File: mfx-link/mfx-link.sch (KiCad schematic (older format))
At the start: 53 parts, among them P1 CONN_01X02, P2 CONN_02X03, P3 CONN_01X02, P4 Grove I2C, P5 IBT-2, P6 CONN_01X02, P7 CONN_01X03, P8 Grove UART, P9 MFX, Q1 BC547, Q2 BC547, Q3 BC547, SW1 SW_PUSH, U1 LM393-1, U2 7805, U3 PIC16F1705, U4 6N137, U5 7805

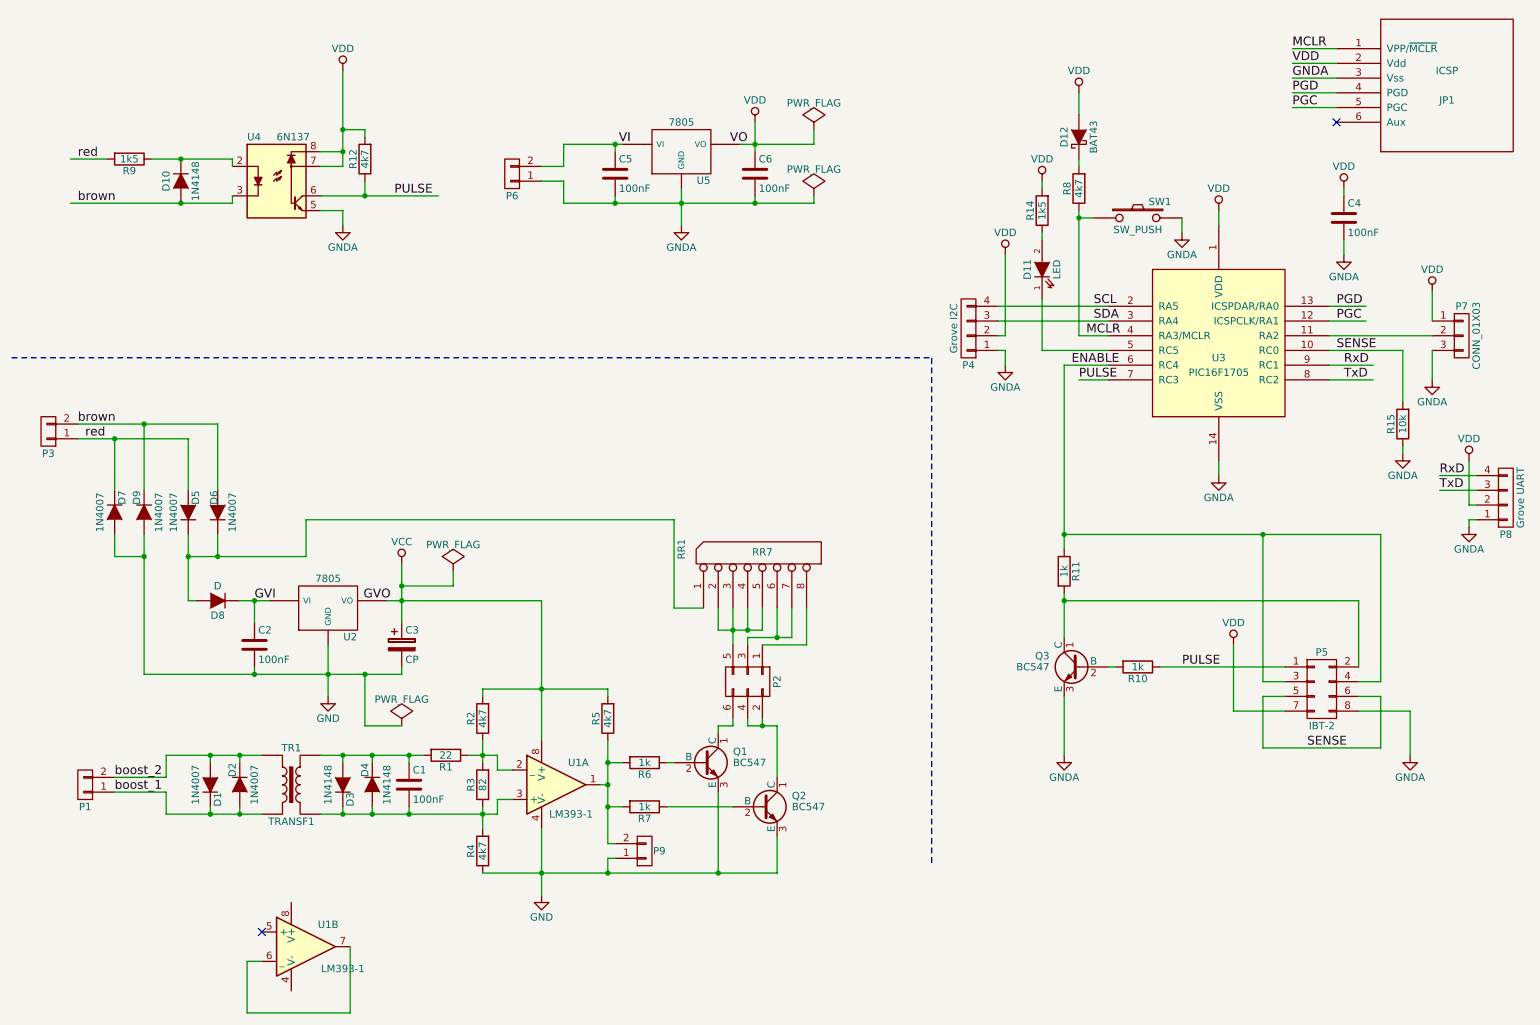
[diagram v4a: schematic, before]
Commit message: fix diodes
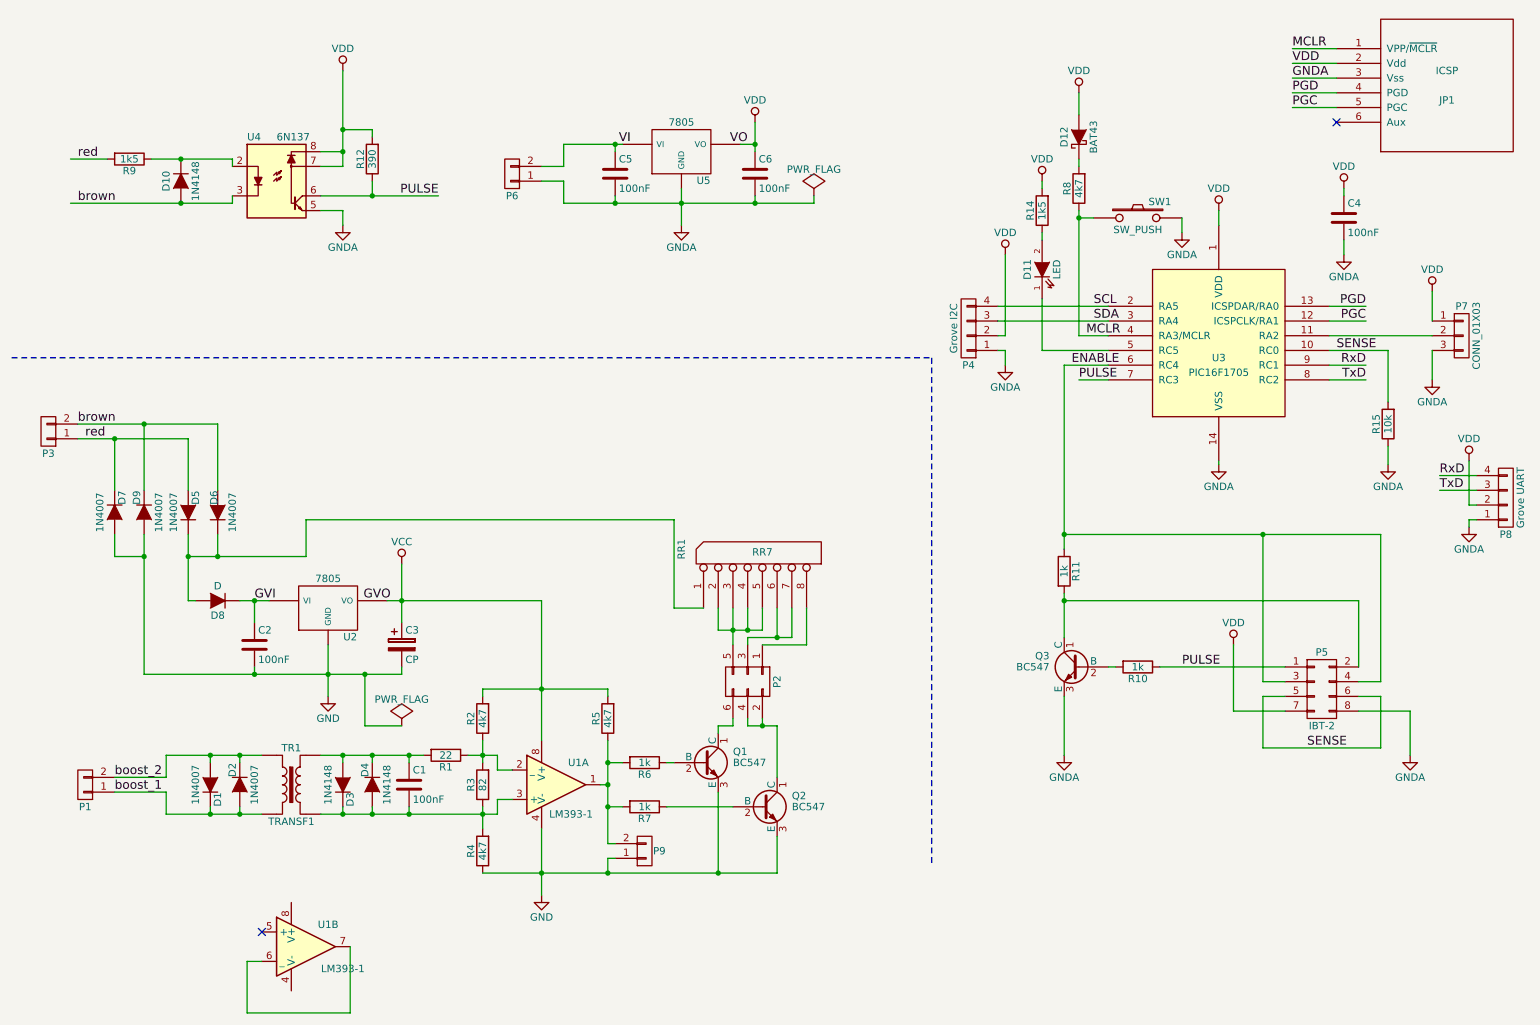
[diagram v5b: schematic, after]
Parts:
- R12: value 4k7 -> 390
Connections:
- wire segments 186 -> 182
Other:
- moved on the sheet: R12, R15
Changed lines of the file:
@@
 Sheet 1 1
 Title "Booster-Link IBT-2"
-Date "03.02.2017"
+Date "2017-04-10"
 Rev "1.0"
 Comp "Gerhard Bertelsmann"
@@
 $Comp
 L PWR_FLAG #FLG04
-U 1 1 5890D427
-P 3700 4450
-F 0 "#FLG04" H 3700 4545 50  0001 C CNN
-F 1 "PWR_FLAG" H 3700 4630 50  0000 C CNN
-F 2 "" H 3700 4450 50  0000 C CNN
-F 3 "" H 3700 4450 50  0000 C CNN
-	1    3700 4450
-	1    0    0    -1
-$EndComp
-$Comp
-L PWR_FLAG #FLG05
 U 1 1 5890D50F
 P 3350 5500
-F 0 "#FLG05" H 3350 5595 50  0001 C CNN
+F 0 "#FLG04" H 3350 5595 50  0001 C CNN
 F 1 "PWR_FLAG" H 3350 5680 50  0000 C CNN
 F 2 "" H 3350 5500 50  0000 C CNN
@@
 $EndComp
 $Comp
-L GNDA #PWR06
+L GNDA #PWR05
 U 1 1 5890E3A7
 P 7450 3050
-F 0 "#PWR06" H 7450 2800 50  0001 C CNN
+F 0 "#PWR05" H 7450 2800 50  0001 C CNN
 F 1 "GNDA" H 7450 2900 50  0000 C CNN
 F 2 "" H 7450 3050 50  0000 C CNN
@@
 $EndComp
 $Comp
-L VDD #PWR07
+L VDD #PWR06
 U 1 1 5890E581
 P 7450 2300
-F 0 "#PWR07" H 7450 2150 50  0001 C CNN
+F 0 "#PWR06" H 7450 2150 50  0001 C CNN
 F 1 "VDD" H 7450 2450 50  0000 C CNN
 F 2 "" H 7450 2300 50  0000 C CNN
@@
 SDA
 $Comp
-L GNDA #PWR08
+L GNDA #PWR07
 U 1 1 5890F719
-P 8900 3800
-F 0 "#PWR08" H 8900 3550 50  0001 C CNN
-F 1 "GNDA" H 8900 3650 50  0000 C CNN
-F 2 "" H 8900 3800 50  0000 C CNN
-F 3 "" H 8900 3800 50  0000 C CNN
-	1    8900 3800
+P 8900 3725
+F 0 "#PWR07" H 8900 3475 50  0001 C CNN
+F 1 "GNDA" H 8900 3575 50  0000 C CNN
+F 2 "" H 8900 3725 50  0000 C CNN
+F 3 "" H 8900 3725 50  0000 C CNN
+	1    8900 3725
 	1    0    0    -1
 $EndComp
@@
 $EndComp
 $Comp
-L VDD #PWR09
+L VDD #PWR08
 U 1 1 58910635
 P 8900 2000
-F 0 "#PWR09" H 8900 1850 50  0001 C CNN
+F 0 "#PWR08" H 8900 1850 50  0001 C CNN
 F 1 "VDD" H 8900 2150 50  0000 C CNN
 F 2 "" H 8900 2000 50  0000 C CNN
@@
 $EndComp
 $Comp
-L VDD #PWR010
+L VDD #PWR09
 U 1 1 5891152D
 P 7950 1200
-F 0 "#PWR010" H 7950 1050 50  0001 C CNN
+F 0 "#PWR09" H 7950 1050 50  0001 C CNN
 F 1 "VDD" H 7950 1350 50  0000 C CNN
 F 2 "" H 7950 1200 50  0000 C CNN
@@
 $EndComp
 $Comp
-L VDD #PWR011
+L VDD #PWR010
 U 1 1 5891F45B
 P 9750 1850
-F 0 "#PWR011" H 9750 1700 50  0001 C CNN
+F 0 "#PWR010" H 9750 1700 50  0001 C CNN
 F 1 "VDD" H 9750 2000 50  0000 C CNN
 F 2 "" H 9750 1850 50  0000 C CNN
@@
 $EndComp
 $Comp
-L GNDA #PWR012
+L GNDA #PWR011
 U 1 1 5891F4CC
 P 9750 2300
-F 0 "#PWR012" H 9750 2050 50  0001 C CNN
+F 0 "#PWR011" H 9750 2050 50  0001 C CNN
 F 1 "GNDA" H 9750 2150 50  0000 C CNN
 F 2 "" H 9750 2300 50  0000 C CNN
@@
 Text Label 9400 1100 0    60   ~ 0
 GNDA
-Text Label 9700 2650 0    60   ~ 0
+Text Label 9900 2650 2    60   ~ 0
 PGD
-Text Label 9700 2750 0    60   ~ 0
+Text Label 9900 2750 2    60   ~ 0
 PGC
 Text Label 9400 1200 0    60   ~ 0
@@
 $EndComp
 $Comp
-L GNDA #PWR013
+L GNDA #PWR012
 U 1 1 589209D0
 P 7850 5700
-F 0 "#PWR013" H 7850 5450 50  0001 C CNN
+F 0 "#PWR012" H 7850 5450 50  0001 C CNN
 F 1 "GNDA" H 7850 5550 50  0000 C CNN
 F 2 "" H 7850 5700 50  0000 C CNN
@@
 ENABLE
 $Comp
-L GNDA #PWR014
+L GNDA #PWR013
 U 1 1 589214FB
 P 10200 5700
-F 0 "#PWR014" H 10200 5450 50  0001 C CNN
+F 0 "#PWR013" H 10200 5450 50  0001 C CNN
 F 1 "GNDA" H 10200 5550 50  0000 C CNN
 F 2 "" H 10200 5700 50  0000 C CNN
@@
 $EndComp
 $Comp
-L VDD #PWR015
+L VDD #PWR014
 U 1 1 5892163B
 P 9000 4950
-F 0 "#PWR015" H 9000 4800 50  0001 C CNN
+F 0 "#PWR014" H 9000 4800 50  0001 C CNN
 F 1 "VDD" H 9000 5100 50  0000 C CNN
 F 2 "" H 9000 4950 50  0000 C CNN
@@
 $EndComp
 $Comp
-L GNDA #PWR016
+L GNDA #PWR015
 U 1 1 5892345E
 P 5250 2100
-F 0 "#PWR016" H 5250 1850 50  0001 C CNN
+F 0 "#PWR015" H 5250 1850 50  0001 C CNN
 F 1 "GNDA" H 5250 1950 50  0000 C CNN
 F 2 "" H 5250 2100 50  0000 C CNN
@@
 $EndComp
 $Comp
-L VDD #PWR017
+L VDD #PWR016
 U 1 1 589234E4
 P 5750 1400
-F 0 "#PWR017" H 5750 1250 50  0001 C CNN
+F 0 "#PWR016" H 5750 1250 50  0001 C CNN
 F 1 "VDD" H 5750 1550 50  0000 C CNN
 F 2 "" H 5750 1400 50  0000 C CNN
@@
 $EndComp
 $Comp
-L PWR_FLAG #FLG018
-U 1 1 5892374C
-P 6150 1450
-F 0 "#FLG018" H 6150 1545 50  0001 C CNN
-F 1 "PWR_FLAG" H 6150 1630 50  0000 C CNN
-F 2 "" H 6150 1450 50  0000 C CNN
-F 3 "" H 6150 1450 50  0000 C CNN
-	1    6150 1450
-	1    0    0    -1
-$EndComp
-$Comp
-L PWR_FLAG #FLG019
+L PWR_FLAG #FLG017
 U 1 1 589238E7
 P 6150 1900
-F 0 "#FLG019" H 6150 1995 50  0001 C CNN
+F 0 "#FLG017" H 6150 1995 50  0001 C CNN
 F 1 "PWR_FLAG" H 6150 2080 50  0000 C CNN
 F 2 "" H 6150 1900 50  0000 C CNN
@@
 boost_1
 $Comp
-L VDD #PWR020
+L VDD #PWR018
 U 1 1 58926B3B
 P 2950 1050
-F 0 "#PWR020" H 2950 900 50  0001 C CNN
+F 0 "#PWR018" H 2950 900 50  0001 C CNN
 F 1 "VDD" H 2950 1200 50  0000 C CNN
 F 2 "" H 2950 1050 50  0000 C CNN
@@
 $EndComp
 $Comp
-L GNDA #PWR021
+L GNDA #PWR019
 U 1 1 58926BCD
 P 2950 2100
-F 0 "#PWR021" H 2950 1850 50  0001 C CNN
+F 0 "#PWR019" H 2950 1850 50  0001 C CNN
 F 1 "GNDA" H 2950 1950 50  0000 C CNN
 F 2 "" H 2950 2100 50  0000 C CNN
@@
 Connection ~ 3350 4650
 Wire Wire Line
-	3700 4450 3700 4550
-Wire Wire Line
-	3700 4550 3350 4550
-Connection ~ 3350 4550
-Wire Wire Line
 	3100 5150 3100 5500
 Wire Wire Line
@@
 	7400 2650 8150 2650
 Wire Wire Line
-	8900 3700 8900 3800
+	8900 3700 8900 3725
 Wire Wire Line
 	8900 2000 8900 2100
@@
 Connection ~ 7850 4650
 Wire Wire Line
-	7550 4900 7550 4900
-Wire Wire Line
 	9350 5300 9200 5300
 Wire Wire Line
@@
 Wire Wire Line
 	4450 1950 6150 1950
-Wire Wire Line
-	5650 1550 6150 1550
 Wire Wire Line
 	4450 1550 4850 1550
@@
 	5250 1850 5250 2100
 Connection ~ 5250 1950
-Wire Wire Line
-	6150 1550 6150 1450
 Wire Wire Line
 	6150 1950 6150 1900
@@
 	2800 1900 3600 1900
 Wire Wire Line
-	3100 1900 3100 1800
+	3150 1900 3150 1800
 Wire Wire Line
 	5200 4100 2700 4100
@@
 L R R12
 U 1 1 5892B196
-P 3100 1650
-F 0 "R12" V 3180 1650 50  0000 C CNN
-F 1 "4k7" V 3100 1650 50  0000 C CNN
-F 2 "w_pth_resistors:RC03" V 3030 1650 50  0001 C CNN
-F 3 "" H 3100 1650 50  0000 C CNN
-	1    3100 1650
+P 3150 1650
+F 0 "R12" V 3230 1650 50  0000 C CNN
+F 1 "390" V 3150 1650 50  0000 C CNN
+F 2 "w_pth_resistors:RC03" V 3080 1650 50  0001 C CNN
+F 3 "" H 3150 1650 50  0000 C CNN
+	1    3150 1650
 	-1   0    0    1
 $EndComp
 Wire Wire Line
-	2950 1450 3100 1450
-Wire Wire Line
-	3100 1450 3100 1500
+	2950 1450 3150 1450
+Wire Wire Line
+	3150 1450 3150 1500
 Connection ~ 2950 1450
-Connection ~ 3100 1900
+Connection ~ 3150 1900
 $Comp
 L CONN_01X03 P7
@@
 Wire Wire Line
 	9850 4650 9850 5100
-Text Label 3300 1900 0    60   ~ 0
+Text Label 3600 1900 2    60   ~ 0
 PULSE
 Text Label 8650 5100 0    60   ~ 0
@@
 L R R15
 U 1 1 5892F2CF
-P 10150 3450
-F 0 "R15" V 10230 3450 50  0000 C CNN
-F 1 "10k" V 10150 3450 50  0000 C CNN
-F 2 "w_pth_resistors:RC03" V 10080 3450 50  0001 C CNN
-F 3 "" H 10150 3450 50  0000 C CNN
-	1    10150 3450
+P 10050 3450
+F 0 "R15" V 10130 3450 50  0000 C CNN
+F 1 "10k" V 10050 3450 50  0000 C CNN
+F 2 "w_pth_resistors:RC03" V 9980 3450 50  0001 C CNN
+F 3 "" H 10050 3450 50  0000 C CNN
+	1    10050 3450
 	-1   0    0    1
 $EndComp
@@
 $EndComp
 $Comp
-L VDD #PWR022
+L VDD #PWR020
 U 1 1 5893057F
 P 7700 1800
-F 0 "#PWR022" H 7700 1650 50  0001 C CNN
+F 0 "#PWR020" H 7700 1650 50  0001 C CNN
 F 1 "VDD" H 7700 1950 50  0000 C CNN
 F 2 "" H 7700 1800 50  0000 C CNN
@@
 	8200 5100 8150 5100
 $Comp
-L VDD #PWR023
+L VDD #PWR021
 U 1 1 589322F2
 P 10350 2550
-F 0 "#PWR023" H 10350 2400 50  0001 C CNN
+F 0 "#PWR021" H 10350 2400 50  0001 C CNN
 F 1 "VDD" H 10350 2700 50  0000 C CNN
 F 2 "" H 10350 2550 50  0000 C CNN
@@
 $EndComp
 $Comp
-L GNDA #PWR024
+L GNDA #PWR022
 U 1 1 58932648
 P 10350 3150
-F 0 "#PWR024" H 10350 2900 50  0001 C CNN
+F 0 "#PWR022" H 10350 2900 50  0001 C CNN
 F 1 "GNDA" H 10350 3000 50  0000 C CNN
 F 2 "" H 10350 3150 50  0000 C CNN
@@
 	10350 2950 10350 3150
 $Comp
-L GNDA #PWR025
+L GNDA #PWR023
 U 1 1 58932E12
-P 10150 3650
-F 0 "#PWR025" H 10150 3400 50  0001 C CNN
-F 1 "GNDA" H 10150 3500 50  0000 C CNN
-F 2 "" H 10150 3650 50  0000 C CNN
-F 3 "" H 10150 3650 50  0000 C CNN
-	1    10150 3650
-	1    0    0    -1
-$EndComp
-Wire Wire Line
-	9650 2950 10150 2950
-Wire Wire Line
-	10150 2950 10150 3300
-Wire Wire Line
-	10150 3600 10150 3650
+P 10050 3725
+F 0 "#PWR023" H 10050 3475 50  0001 C CNN
+F 1 "GNDA" H 10050 3575 50  0000 C CNN
+F 2 "" H 10050 3725 50  0000 C CNN
+F 3 "" H 10050 3725 50  0000 C CNN
+	1    10050 3725
+	1    0    0    -1
+$EndComp
+Wire Wire Line
+	9650 2950 10050 2950
+Wire Wire Line
+	10050 2950 10050 3300
+Wire Wire Line
+	10050 3600 10050 3725
 NoConn ~ 2400 6900
 Wire Notes Line
@@
 	6950 3000 6950 6450
 Wire Wire Line
-	9650 3050 9950 3050
-Wire Wire Line
-	9650 3150 9950 3150
-Text Label 9750 3050 0    60   ~ 0
+	9650 3050 9900 3050
+Wire Wire Line
+	9650 3150 9900 3150
+Text Label 9900 3050 2    60   ~ 0
 RxD
-Text Label 9750 3150 0    60   ~ 0
+Text Label 9900 3150 2    60   ~ 0
 TxD
 $Comp
@@
 $EndComp
 $Comp
-L GNDA #PWR026
+L GNDA #PWR024
 U 1 1 5893744C
 P 10600 4150
-F 0 "#PWR026" H 10600 3900 50  0001 C CNN
+F 0 "#PWR024" H 10600 3900 50  0001 C CNN
 F 1 "GNDA" H 10600 4000 50  0000 C CNN
 F 2 "" H 10600 4150 50  0000 C CNN
@@
 $EndComp
 $Comp
-L VDD #PWR027
+L VDD #PWR025
 U 1 1 58937D09
 P 10600 3700
-F 0 "#PWR027" H 10600 3550 50  0001 C CNN
+F 0 "#PWR025" H 10600 3550 50  0001 C CNN
 F 1 "VDD" H 10600 3850 50  0000 C CNN
 F 2 "" H 10600 3700 50  0000 C CNN
@@
 $EndComp
 $Comp
-L GNDA #PWR028
+L GNDA #PWR026
 U 1 1 5893AE37
 P 8650 2150
-F 0 "#PWR028" H 8650 1900 50  0001 C CNN
+F 0 "#PWR026" H 8650 1900 50  0001 C CNN
 F 1 "GNDA" H 8650 2000 50  0000 C CNN
 F 2 "" H 8650 2150 50  0000 C CNN
@@
 Text Label 3275 4650 2    60   ~ 0
 GVO
+Wire Wire Line
+	5650 1550 5750 1550
 $EndSCHEMATC

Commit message: fix diode pins
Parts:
- D1, D10, D2, D3, D4, D5, D6, D7, D8, D9: symbol D -> D-RESCUE-mfx-link
- D12: symbol D_Schottky -> D_Schottky-RESCUE-mfx-link
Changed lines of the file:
@@
 $EndComp
 $Comp
-L D D1
+L D-RESCUE-mfx-link D1
 U 1 1 586FB141
 P 2050 5900
@@
 $EndComp
 $Comp
-L D D2
+L D-RESCUE-mfx-link D2
 U 1 1 586FB1AE
 P 2250 5900
@@
 $EndComp
 $Comp
-L D D3
+L D-RESCUE-mfx-link D3
 U 1 1 586FB68D
 P 2950 5900
@@
 $EndComp
 $Comp
-L D D4
+L D-RESCUE-mfx-link D4
 U 1 1 586FB6CE
 P 3150 5900
@@
 $EndComp
 $Comp
-L D D8
+L D-RESCUE-mfx-link D8
 U 1 1 5890CAEB
 P 2100 4650
@@
 $EndComp
 $Comp
-L D D5
+L D-RESCUE-mfx-link D5
 U 1 1 5890D6E1
 P 1900 4050
@@
 $EndComp
 $Comp
-L D D6
+L D-RESCUE-mfx-link D6
 U 1 1 5890D779
 P 2100 4050
@@
 $EndComp
 $Comp
-L D D7
+L D-RESCUE-mfx-link D7
 U 1 1 5890D818
 P 1400 4050
@@
 $EndComp
 $Comp
-L D D9
+L D-RESCUE-mfx-link D9
 U 1 1 5890D8AE
 P 1600 4050
@@
 $EndComp
 $Comp
-L D D10
+L D-RESCUE-mfx-link D10
 U 1 1 5892404C
 P 1850 1800
@@
 TxD
 $Comp
-L D_Schottky D12
+L D_Schottky-RESCUE-mfx-link D12
 U 1 1 589396E9
 P 7950 1500

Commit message: fix BC547 pinning
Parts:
- Q1, Q2, Q3: footprint w_to:to92_3 -> TO_SOT_Packages_THT:TO-92_Inline_Narrow_Oval
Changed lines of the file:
@@
 F 0 "Q1" H 5600 5825 50  0000 L CNN
 F 1 "BC547" H 5600 5750 50  0000 L CNN
-F 2 "w_to:to92_3" H 5600 5675 50  0001 L CIN
+F 2 "TO_SOT_Packages_THT:TO-92_Inline_Narrow_Oval" H 5600 5675 50  0001 L CIN
 F 3 "" H 5400 5750 50  0000 L CNN
 	1    5400 5750
@@
 F 0 "Q2" H 6000 6125 50  0000 L CNN
 F 1 "BC547" H 6000 6050 50  0000 L CNN
-F 2 "w_to:to92_3" H 6000 5975 50  0001 L CIN
+F 2 "TO_SOT_Packages_THT:TO-92_Inline_Narrow_Oval" H 6000 5975 50  0001 L CIN
 F 3 "" H 5800 6050 50  0000 L CNN
 	1    5800 6050
@@
 F 0 "Q3" H 8150 5175 50  0000 L CNN
 F 1 "BC547" H 8150 5100 50  0000 L CNN
-F 2 "w_to:to92_3" H 8150 5025 50  0001 L CIN
+F 2 "TO_SOT_Packages_THT:TO-92_Inline_Narrow_Oval" H 8150 5025 50  0001 L CIN
 F 3 "" H 7950 5100 50  0000 L CNN
 	1    7950 5100

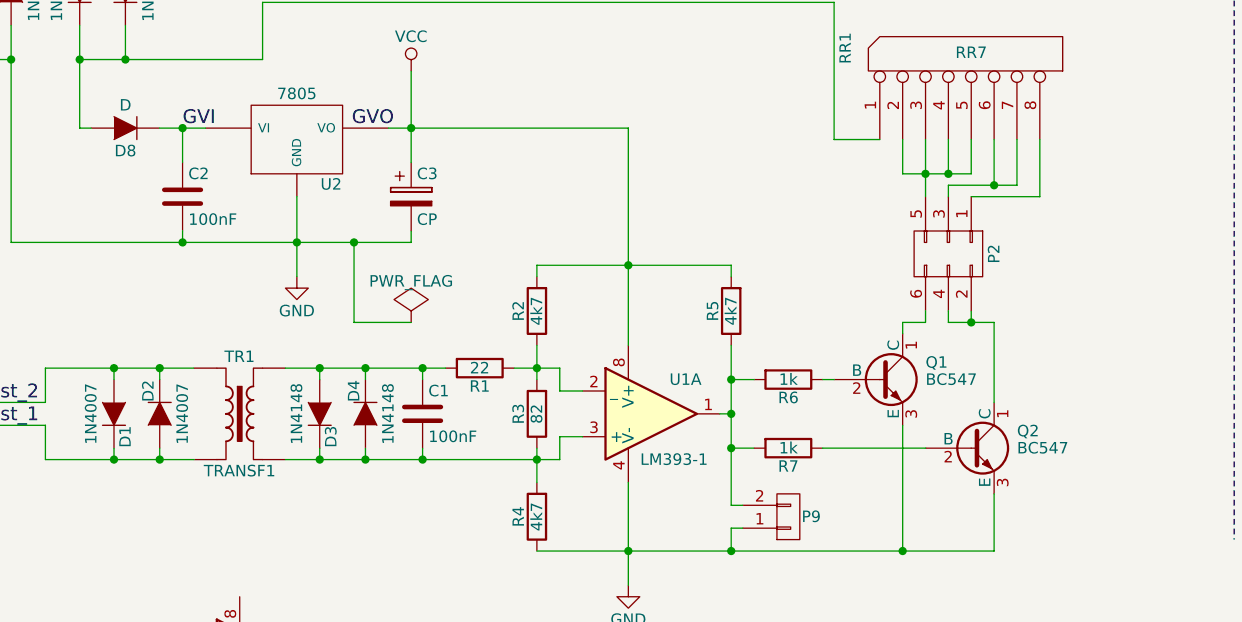
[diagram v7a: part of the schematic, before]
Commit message: change caps
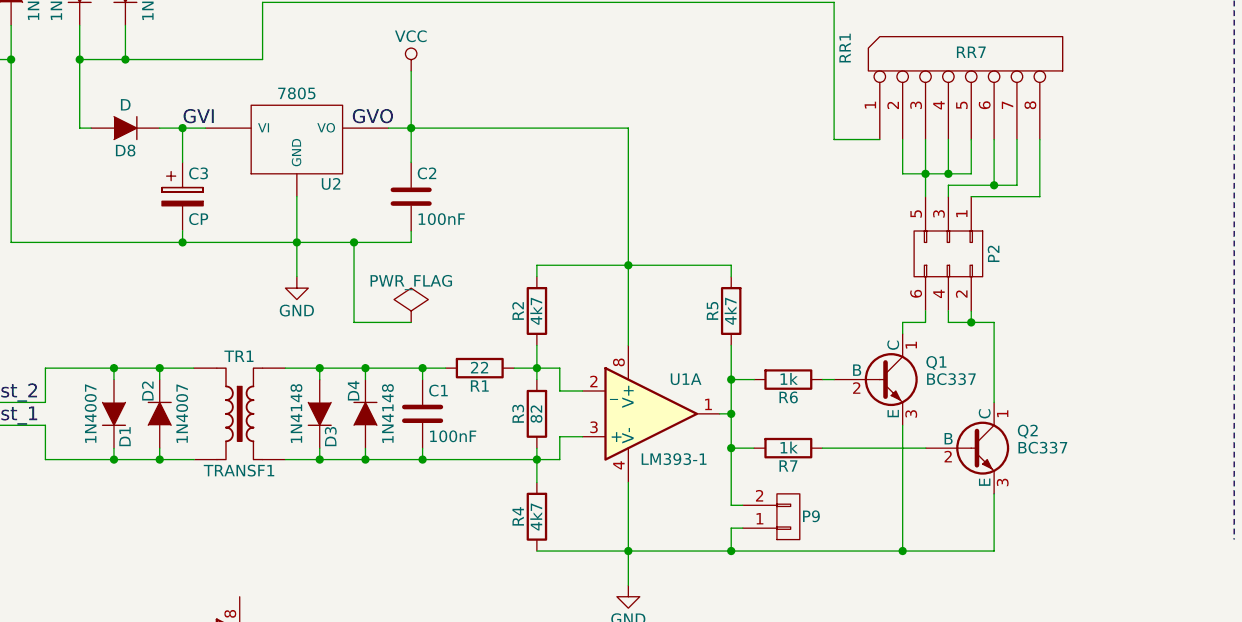
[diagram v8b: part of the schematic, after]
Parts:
- Q1, Q2: value BC547 -> BC337
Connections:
- net GVI: now also C3.1; no longer C2.1
- net VCC: now also C2.1; no longer C3.1
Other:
- moved on the sheet: C2, C3
